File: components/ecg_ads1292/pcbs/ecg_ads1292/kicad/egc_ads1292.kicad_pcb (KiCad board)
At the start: 2 copper layers, 105 x 52.5 mm, 92 parts, among them IC1 ADS1292, J1 n.p., J2 n.p., J3 n.p., J4 n.p., J5 Conn_02x06_Odd_Even, U1 TPS73033DBVT

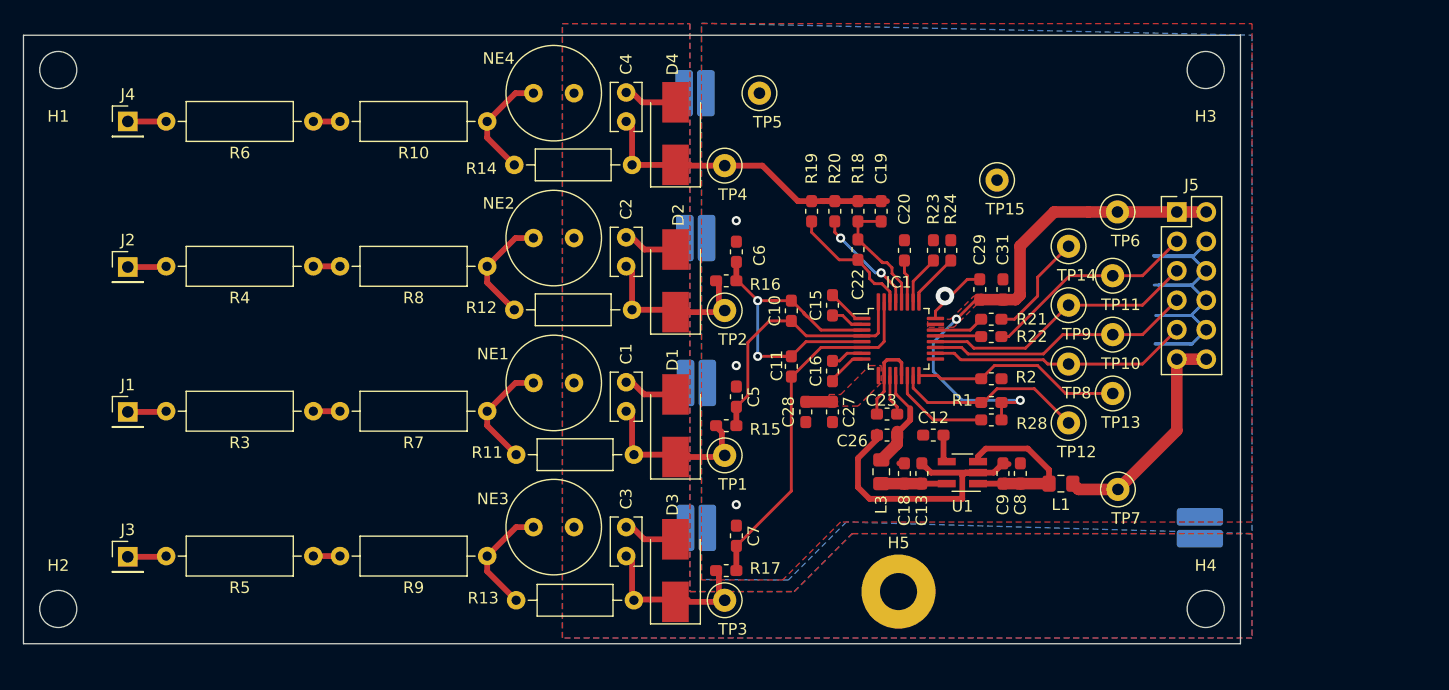
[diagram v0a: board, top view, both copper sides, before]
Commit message: allow daisy chaining and improve ground planes
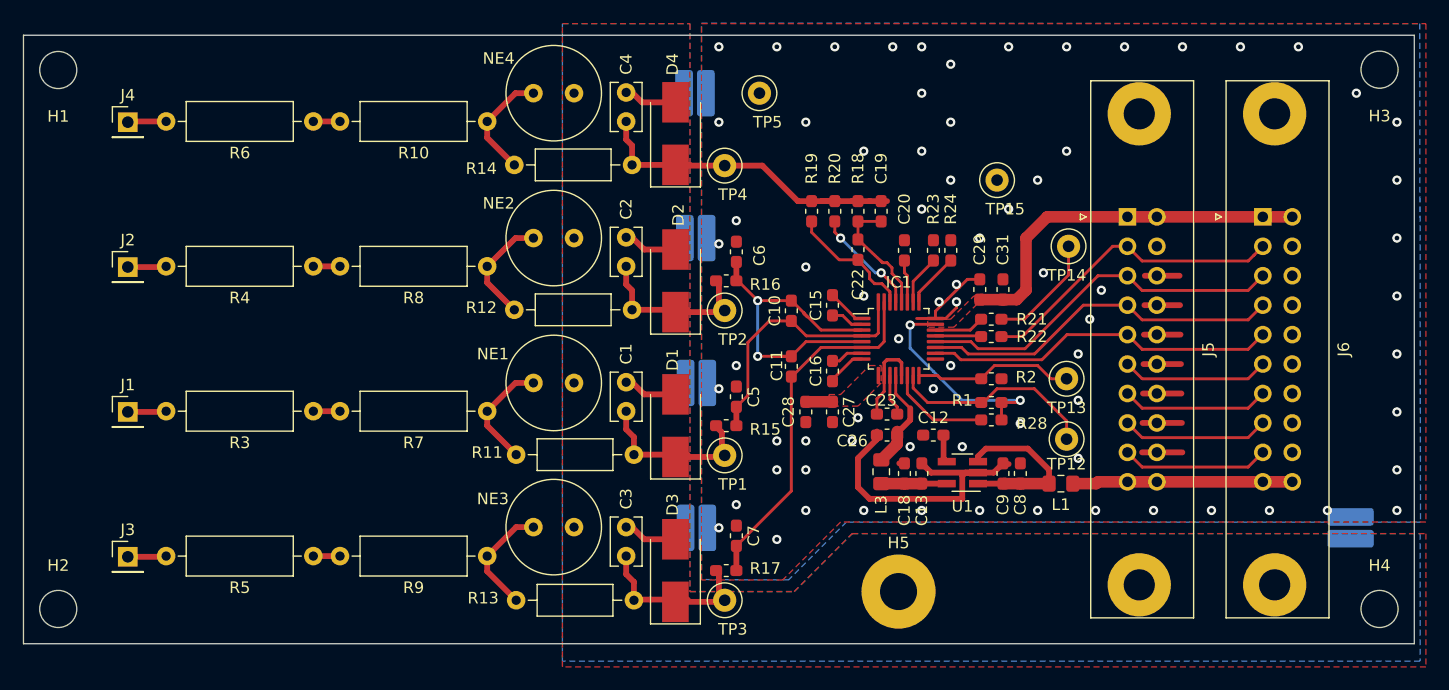
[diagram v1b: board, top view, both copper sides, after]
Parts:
- removed TP10, TP11, TP6, TP7, TP8, TP9: , TestPoint:TestPoint_Loop_D2.50mm_Drill1.0mm
- added J6: Conn_02x10_Odd_Even, Connector_IDC:IDC-Header_2x10_P2.54mm_Vertical_Lock, F.Cu at (144.4, 113.2)
- J5: value Conn_02x06_Odd_Even -> Conn_02x10_Odd_Even; footprint Connector_PinHeader_2.54mm:PinHeader_2x06_P2.54mm_Vertical -> Connector_IDC:IDC-Header_2x10_P2.54mm_Vertical_Lock
- moved H3 15.0 mm to (154.5, 100.5)
- moved H4 15.0 mm to (154.5, 147.0)
- moved R30 13.0 mm to (152.0, 140.0)
- moved J5 4.28 mm to (132.8, 113.2)
- moved TP13 4.18 mm to (127.5, 127.1)
- moved TP12 1.41 mm to (127.5, 132.3)
- moved J4 0.06 mm to (46.5, 105.0)
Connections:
- net /DIN renamed /MOSI
- net /DOUT renamed /MISO
- net /~CS renamed /~CS_ECG
- J5 pad 11: /5V -> /~CS_PPG
- J5 pad 12: /5V -> GND
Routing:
- net /SDA: track 0.00 -> 12.7 mm
- net /~CS_BPR: track 0.00 -> 12.7 mm
- net /~CS_PPG: track 0.00 -> 12.7 mm
- net /SCL: track 0.00 -> 12.7 mm
- net GND: track 78.2 -> 67.1 mm, vias 4 -> 72
- net /SCLK: track 23.8 -> 32.2 mm
- net /MISO: track 18.5 -> 26.8 mm
- net /MOSI: track 23.0 -> 31.3 mm
- net /~CS_ECG: track 22.4 -> 30.4 mm
- net /3V3: track 44.9 -> 51.3 mm
- net /START: track 18.3 -> 13.8 mm
- net /~PDN_RESET: track 16.7 -> 18.0 mm
- net /5V: track 20.0 -> 19.0 mm
- net /~DRDY: track 9.35 -> 9.85 mm
- net (no net): vias 0 -> 1
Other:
- board size 105 x 52.5 mm -> 120 x 52.5 mm

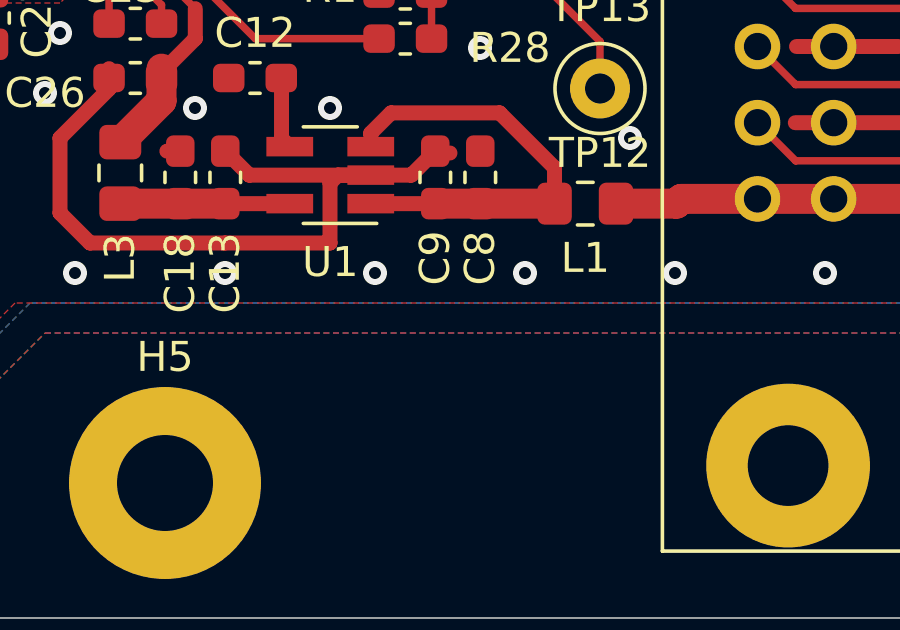
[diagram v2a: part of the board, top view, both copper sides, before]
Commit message: add gnd/gndpwr bridge at analog power supply
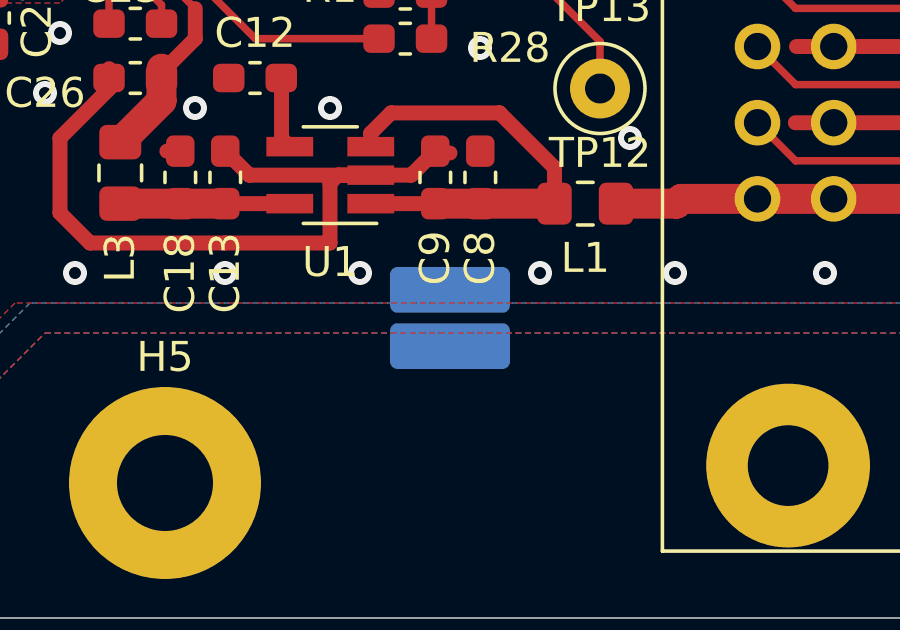
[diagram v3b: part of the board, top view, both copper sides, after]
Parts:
- added R31: n.p., Resistor_SMD:R_0815_2038Metric_Pad1.53x4.00mm_HandSolder, B.Cu at (122.5, 140.0)
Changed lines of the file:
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@@
     (tracks 403)
     (zones 0)
-    (modules 87)
+    (modules 88)
     (nets 55)
   )
@@
     (add_net /out_rld)
   )
+  (module Resistor_SMD:R_0815_2038Metric_Pad1.53x4.00mm_HandSolder (layer B.Cu)
+    (at 122.5 140 270)
+    (descr "Resistor SMD 0815 (2038 Metric), square (rectangular) end terminal, IPC_7351 nominal with elongated pad for handsoldering. (Body size source: http://www.yageo.com/documents/recent/PYu-PRPFPH_521_RoHS_L_0.pdf), generated with kicad-footprint-generator")
+    (tags "resistor handsolder")
+    (attr smd)
+    (fp_text reference R31 (at 0 2.95 270) (layer B.SilkS)
+      (effects (font (size 1 1) (thickness 0.15)) (justify mirror))
+    )
+    (fp_text value n.p. (at 0 -2.95 270) (layer B.Fab)
+      (effects (font (size 1 1) (thickness 0.15)) (justify mirror))
+    )
+    (fp_text user %R (at 0 0 270) (layer B.Fab)
+      (effects (font (size 0.54 0.54) (thickness 0.08)) (justify mirror))
+    )
+    (fp_line (start 1.95 -2.25) (end -1.95 -2.25) (layer B.CrtYd) (width 0.05))
+    (fp_line (start 1.95 2.25) (end 1.95 -2.25) (layer B.CrtYd) (width 0.05))
+    (fp_line (start -1.95 2.25) (end 1.95 2.25) (layer B.CrtYd) (width 0.05))
+    (fp_line (start -1.95 -2.25) (end -1.95 2.25) (layer B.CrtYd) (width 0.05))
+    (fp_line (start 1.075 -1.875) (end -1.075 -1.875) (layer B.Fab) (width 0.1))
+    (fp_line (start 1.075 1.875) (end 1.075 -1.875) (layer B.Fab) (width 0.1))
+    (fp_line (start -1.075 1.875) (end 1.075 1.875) (layer B.Fab) (width 0.1))
+    (fp_line (start -1.075 -1.875) (end -1.075 1.875) (layer B.Fab) (width 0.1))
+    (pad 2 smd roundrect (at 0.9375 0 270) (size 1.525 4) (layers B.Cu B.Paste B.Mask) (roundrect_rratio 0.163934)
+      (net 47 GNDPWR))
+    (pad 1 smd roundrect (at -0.9375 0 270) (size 1.525 4) (layers B.Cu B.Paste B.Mask) (roundrect_rratio 0.163934)
+      (net 2 GND))
+    (model ${KISYS3DMOD}/Resistor_SMD.3dshapes/R_0815_2038Metric.wrl
+      (at (xyz 0 0 0))
+      (scale (xyz 1 1 1))
+      (rotate (xyz 0 0 0))
+    )
+  )
   (module Connector_IDC:IDC-Header_2x10_P2.54mm_Vertical_Lock (layer F.Cu)
     (at 132.75 113.17)
@@
   (via (at 135 138.5) (size 0.8) (drill 0.4) (layers F.Cu B.Cu) (net 2))
   (via (at 130 138.5) (size 0.8) (drill 0.4) (layers F.Cu B.Cu) (net 2))
-  (via (at 125 138.5) (size 0.8) (drill 0.4) (layers F.Cu B.Cu) (net 2))
-  (via (at 120 138.5) (size 0.8) (drill 0.4) (layers F.Cu B.Cu) (net 2))
+  (via (at 125.5 138.5) (size 0.8) (drill 0.4) (layers F.Cu B.Cu) (net 2))
+  (via (at 119.5 138.5) (size 0.8) (drill 0.4) (layers F.Cu B.Cu) (net 2))
   (segment (start 115 137.5) (end 118.5 137.5) (width 0.5) (layer F.Cu) (net 2))
   (via (at 115 138.5) (size 0.8) (drill 0.4) (layers F.Cu B.Cu) (net 2))

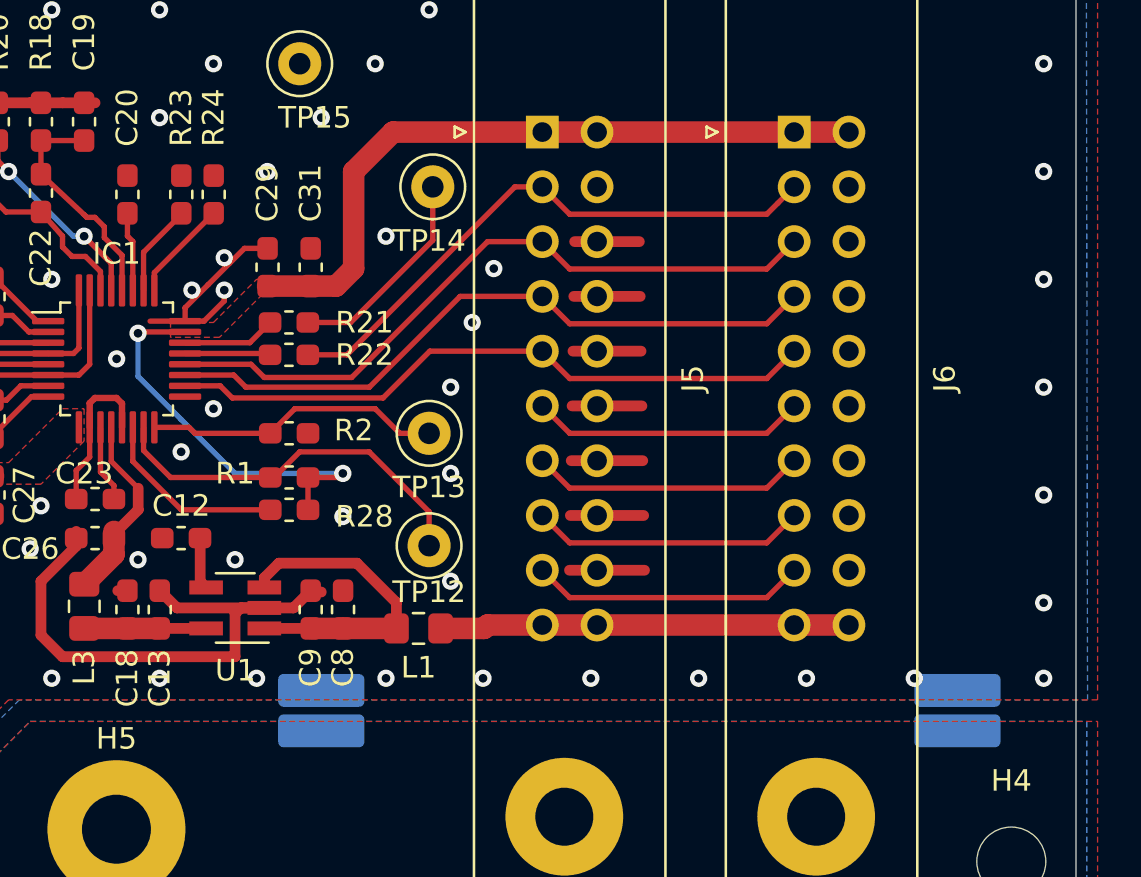
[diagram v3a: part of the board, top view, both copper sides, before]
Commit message: add board name and version to pcb
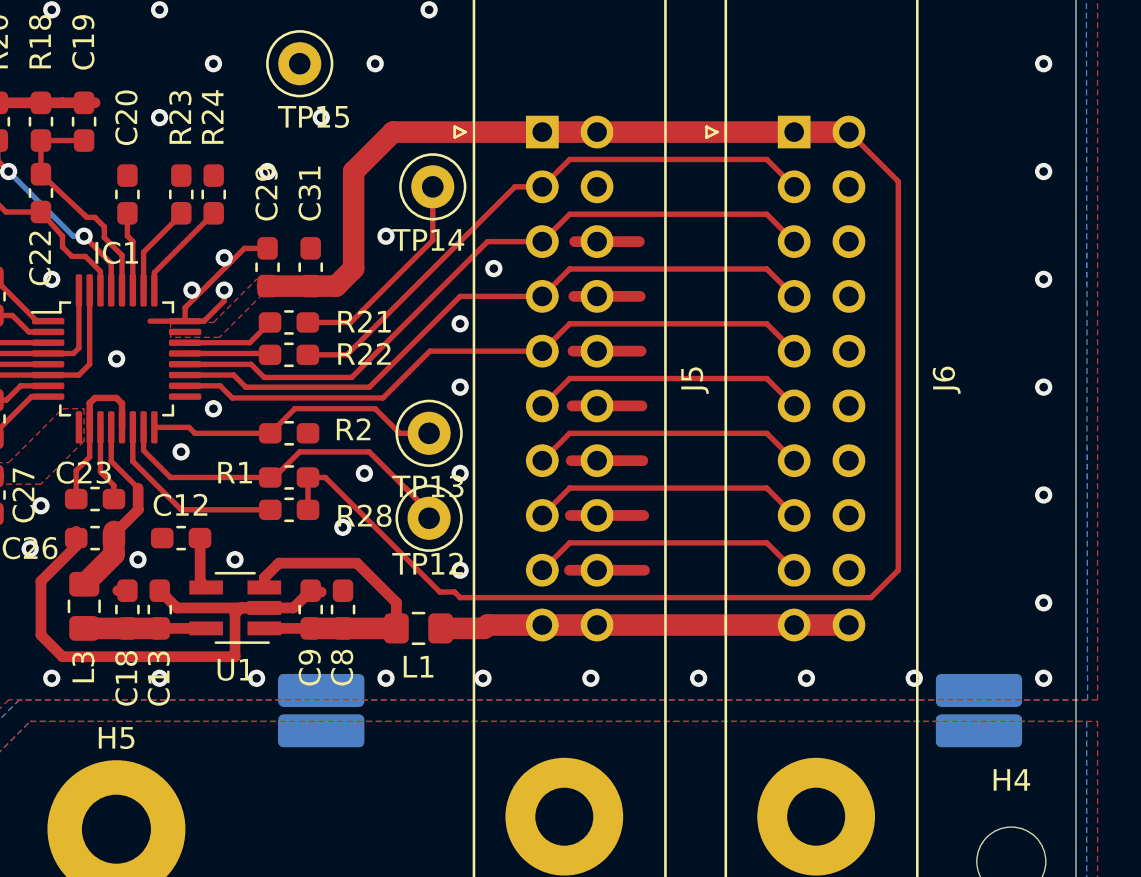
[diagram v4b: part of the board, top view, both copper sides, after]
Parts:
- moved TP12 1.27 mm to (127.5, 131.1)
- moved R30 1.00 mm to (153.0, 140.0)
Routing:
- net /3V3: track 51.3 -> 85.5 mm, vias 2 -> 0
- net GND: vias 72 -> 74
- net (no net): vias 1 -> 0
